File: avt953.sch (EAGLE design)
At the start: 51 parts, among them CON3 RJ45-6L2-B, CON4A MKDS_5/3-6,35, CON4B MKDS_5/3-6,35, CON4C MKDS_5/3-6,35, CON4D MKDS_5/3-6,35, X1 20MHz, X2 20MHz

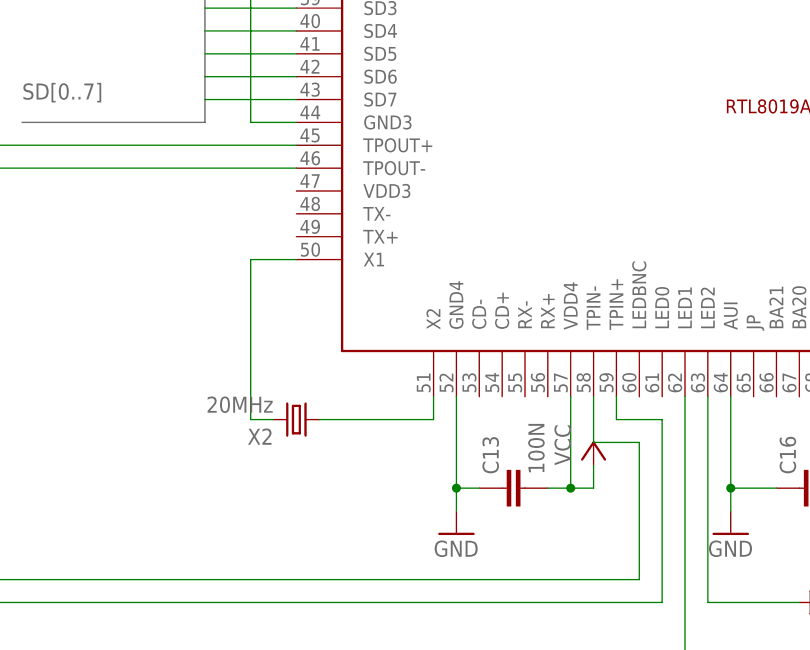
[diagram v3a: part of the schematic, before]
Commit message: Przeprowadzono test ERC na schemacie i poprawiono zaraportowane błędy.
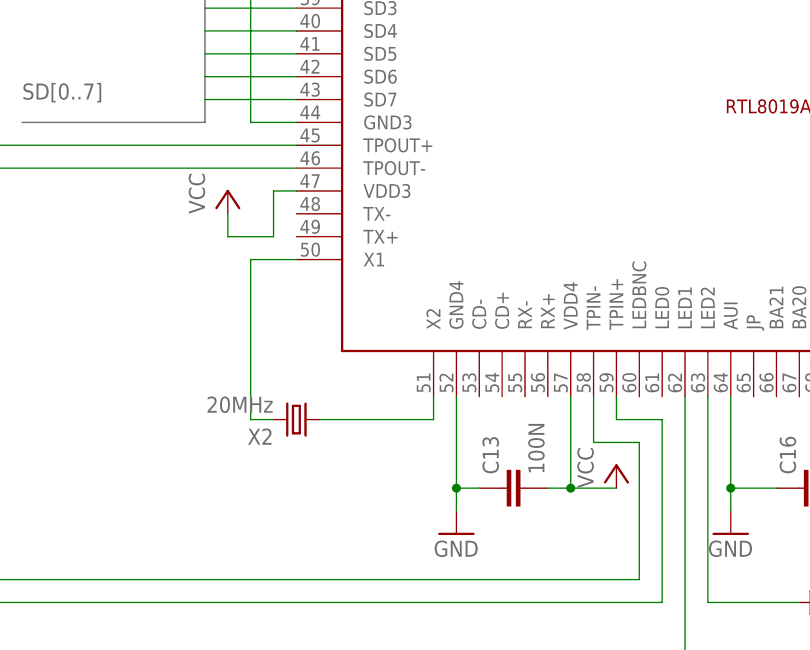
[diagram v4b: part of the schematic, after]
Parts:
- C1, C3: device resistor:CPOL-EUE5-13 -> resistor:CPOL-EUTT2D5
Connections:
- net VCC: now also US5.VDD3
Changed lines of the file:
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@@
 <part name="GND3" library="supply1" deviceset="GND" device=""/>
 <part name="D1" library="diode" deviceset="1N4148" device="DO35-10" value="1N4147"/>
-<part name="C1" library="resistor" deviceset="CPOL-EU" device="E5-13" value="100u"/>
-<part name="C3" library="resistor" deviceset="CPOL-EU" device="E5-13" value="220u"/>
+<part name="C1" library="resistor" deviceset="CPOL-EU" device="TT2D5" value="100u"/>
+<part name="C3" library="resistor" deviceset="CPOL-EU" device="TT2D5" value="220u"/>
 <part name="C2" library="resistor" deviceset="C-EU" device="C1206K" value="100n"/>
 <part name="GND4" library="supply1" deviceset="GND" device=""/>
@@
 <part name="GND23" library="supply1" deviceset="GND" device=""/>
 <part name="FRAME1" library="frames" deviceset="FRAME_B_L" device=""/>
+<part name="P+16" library="supply1" deviceset="VCC" device=""/>
 </parts>
 <sheets>
@@
 <instance part="C15" gate="G$1" x="297.18" y="187.96"/>
 <instance part="GND13" gate="1" x="200.66" y="139.7"/>
-<instance part="P+6" gate="VCC" x="215.9" y="149.86"/>
+<instance part="P+6" gate="VCC" x="218.44" y="147.32"/>
 <instance part="C13" gate="G$1" x="205.74" y="144.78" rot="R90"/>
 <instance part="C16" gate="G$1" x="238.76" y="144.78" rot="R90"/>
@@
 <instance part="FRAME1" gate="G$1" x="0" y="0"/>
 <instance part="FRAME1" gate="G$2" x="325.12" y="0"/>
+<instance part="P+16" gate="VCC" x="175.26" y="177.8"/>
 </instances>
 <busses>
@@
 <wire x1="213.36" y1="154.94" x2="213.36" y2="144.78" width="0.1524" layer="91"/>
 <pinref part="P+6" gate="VCC" pin="VCC"/>
-<wire x1="213.36" y1="144.78" x2="215.9" y2="144.78" width="0.1524" layer="91"/>
-<wire x1="215.9" y1="144.78" x2="215.9" y2="147.32" width="0.1524" layer="91"/>
+<wire x1="213.36" y1="144.78" x2="218.44" y2="144.78" width="0.1524" layer="91"/>
 <junction x="213.36" y="144.78"/>
 </segment>
@@
 <wire x1="271.78" y1="50.8" x2="274.32" y2="50.8" width="0.1524" layer="91"/>
 <wire x1="274.32" y1="50.8" x2="274.32" y2="55.88" width="0.1524" layer="91"/>
+</segment>
+<segment>
+<pinref part="P+16" gate="VCC" pin="VCC"/>
+<wire x1="175.26" y1="175.26" x2="175.26" y2="172.72" width="0.1524" layer="91"/>
+<wire x1="175.26" y1="172.72" x2="180.34" y2="172.72" width="0.1524" layer="91"/>
+<wire x1="180.34" y1="172.72" x2="180.34" y2="177.8" width="0.1524" layer="91"/>
+<pinref part="US5" gate="G$1" pin="VDD3"/>
+<wire x1="180.34" y1="177.8" x2="182.88" y2="177.8" width="0.1524" layer="91"/>
 </segment>
 </net>
@@
 </sheet>
 </sheets>
+<errors>
+</errors>
 </schematic>
 </drawing>

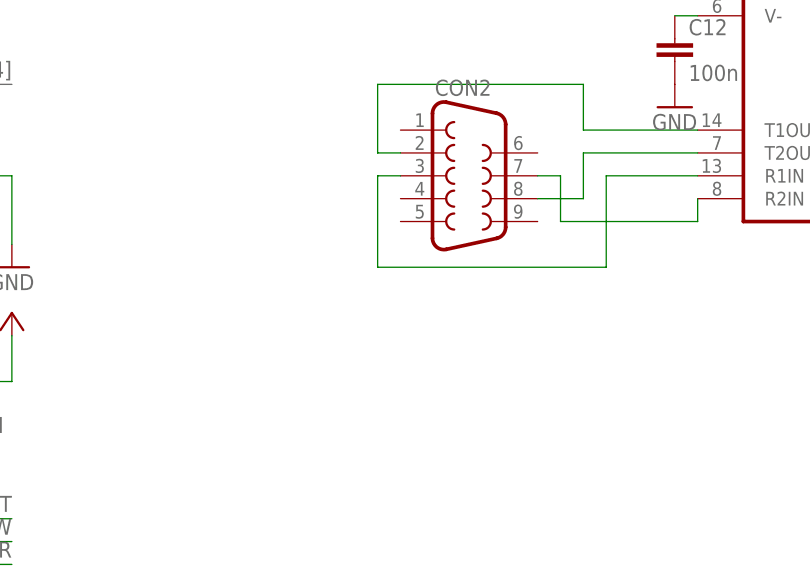
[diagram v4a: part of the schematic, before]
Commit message: Nie było połączenia z masą w konektorze RS232.
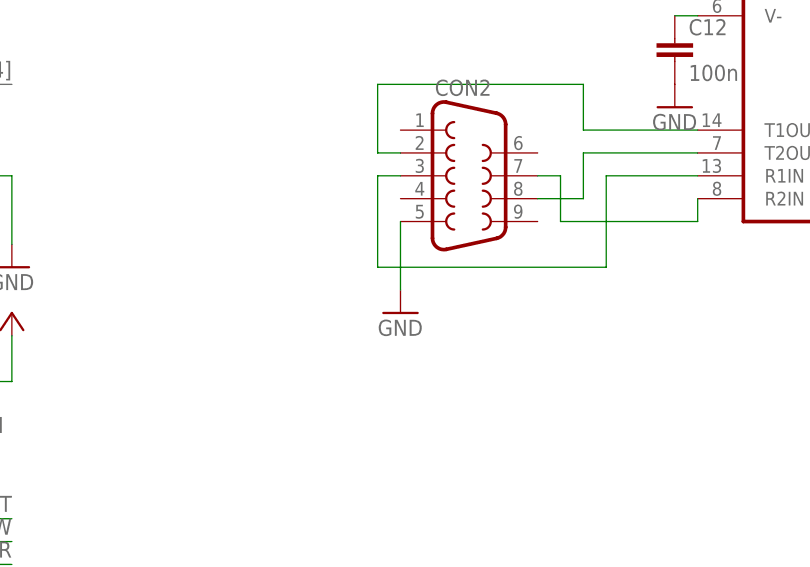
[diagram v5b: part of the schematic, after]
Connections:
- net GND: now also CON2.5
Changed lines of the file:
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@@
 <part name="FRAME1" library="frames" deviceset="FRAME_B_L" device=""/>
 <part name="P+16" library="supply1" deviceset="VCC" device=""/>
+<part name="GND24" library="supply1" deviceset="GND" device=""/>
 </parts>
 <sheets>
@@
 <instance part="FRAME1" gate="G$2" x="325.12" y="0"/>
 <instance part="P+16" gate="VCC" x="175.26" y="177.8"/>
+<instance part="GND24" gate="1" x="317.5" y="58.42"/>
 </instances>
 <busses>
@@
 <junction x="266.7" y="73.66"/>
 </segment>
+<segment>
+<pinref part="GND24" gate="1" pin="GND"/>
+<pinref part="CON2" gate="G$1" pin="5"/>
+<wire x1="317.5" y1="60.96" x2="317.5" y2="68.58" width="0.1524" layer="91"/>
+</segment>
 </net>
